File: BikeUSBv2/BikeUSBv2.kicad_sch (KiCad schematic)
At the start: 50 parts, among them J1 TYPE-C-31-M-16, J2 Conn_01x02_Female, Q1 MMBT3906, SW1 SW_Push, SW2 SW_Push, U1 TPS63020DSJR, U2 ATtiny1616-M

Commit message: all parts selected
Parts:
- D1: value yellow -> XL-2012UOC; LCSC (none) -> C965813
- D10: now not fitted; now left out of the parts list
- D2: value green -> XL-2012UGC; LCSC (none) -> C965815
- D3: value blue -> XL-2012UBC; LCSC (none) -> C965817
- D9: value red -> XL-2012SURC; LCSC (none) -> C965812
- J2: value Conn_01x02_Female -> JST S2B-EH(LF)(SN); LCSC (none) -> C514173
- SW1, SW2: value SW_Push -> 1TS002E-2500-2501-CT; LCSC (none) -> C255802
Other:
- moved on the sheet: SW1, SW2
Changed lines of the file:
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@@
     (stroke (width 0) (type default))
   )
-  (wire (pts (xy 103.505 181.61) (xy 106.68 181.61))
+  (wire (pts (xy 109.22 181.61) (xy 112.395 181.61))
     (stroke (width 0) (type default))
   )
@@
     (stroke (width 0) (type default))
   )
-  (wire (pts (xy 103.505 175.26) (xy 106.68 175.26))
+  (wire (pts (xy 109.22 175.26) (xy 112.395 175.26))
     (stroke (width 0) (type default))
   )
@@
     (effects (font (size 1.27 1.27)) (justify right bottom))
   )
-  (label "S2" (at 103.505 181.61 0) (fields_autoplaced)
+  (label "S2" (at 109.22 181.61 0) (fields_autoplaced)
     (effects (font (size 1.27 1.27)) (justify left bottom))
   )
@@
     (effects (font (size 1.27 1.27)) (justify right bottom))
   )
-  (label "S1" (at 103.505 175.26 0) (fields_autoplaced)
+  (label "S1" (at 109.22 175.26 0) (fields_autoplaced)
     (effects (font (size 1.27 1.27)) (justify left bottom))
   )
@@
       (effects (font (size 1.27 1.27)) (justify right))
     )
-    (property "Value" "red" (at 90.805 175.26 0)
+    (property "Value" "XL-2012SURC" (at 90.805 175.26 0)
       (effects (font (size 1.27 1.27)) (justify right))
     )
@@
       (effects (font (size 1.27 1.27)) hide)
     )
+    (property "LCSC" "C965812" (at 88.265 179.07 0)
+      (effects (font (size 1.27 1.27)) hide)
+    )
     (pin "2")
     (pin "1")
@@
   )
   (symbol (lib_id "Device:D_Schottky") (at 85.09 126.365 270) (unit 1)
-    (in_bom yes) (on_board yes) (dnp no)
+    (in_bom no) (on_board yes) (dnp yes)
     (property "Reference" "D10" (at 82.55 124.46 0)
       (effects (font (size 1.27 1.27)) (justify left))
@@
     )
   )
-  (symbol (lib_id "Switch:SW_Push") (at 111.76 181.61 0) (unit 1)
-    (in_bom yes) (on_board yes) (dnp no)
-    (property "Reference" "SW2" (at 111.76 183.515 0)
-      (effects (font (size 1.27 1.27)))
-    )
-    (property "Value" "SW_Push" (at 111.76 185.42 0)
-      (effects (font (size 1.27 1.27)))
-    )
-    (property "Footprint" "Button_Switch_SMD:SW_SPST_CK_RS282G05A3" (at 111.76 176.53 0)
-      (effects (font (size 1.27 1.27)) hide)
-    )
-    (property "Datasheet" "~" (at 111.76 176.53 0)
+  (symbol (lib_id "Switch:SW_Push") (at 117.475 181.61 0) (unit 1)
+    (in_bom yes) (on_board yes) (dnp no)
+    (property "Reference" "SW2" (at 117.475 183.515 0)
+      (effects (font (size 1.27 1.27)))
+    )
+    (property "Value" "1TS002E-2500-2501-CT" (at 117.475 185.42 0)
+      (effects (font (size 1.27 1.27)))
+    )
+    (property "Footprint" "Button_Switch_SMD:SW_SPST_CK_RS282G05A3" (at 117.475 176.53 0)
+      (effects (font (size 1.27 1.27)) hide)
+    )
+    (property "Datasheet" "~" (at 117.475 176.53 0)
+      (effects (font (size 1.27 1.27)) hide)
+    )
+    (property "LCSC" "C255802" (at 117.475 181.61 0)
       (effects (font (size 1.27 1.27)) hide)
     )
@@
       (effects (font (size 1.27 1.27)) (justify right))
     )
-    (property "Value" "green" (at 129.54 100.6475 90)
+    (property "Value" "XL-2012UGC" (at 129.54 100.6475 90)
       (effects (font (size 1.27 1.27)) (justify right))
     )
@@
     )
     (property "Datasheet" "~" (at 125.73 97.79 0)
+      (effects (font (size 1.27 1.27)) hide)
+    )
+    (property "LCSC" "C965815" (at 125.73 97.79 90)
       (effects (font (size 1.27 1.27)) hide)
     )
@@
     )
   )
-  (symbol (lib_id "Switch:SW_Push") (at 111.76 175.26 0) (unit 1)
-    (in_bom yes) (on_board yes) (dnp no)
-    (property "Reference" "SW1" (at 111.76 168.91 0)
-      (effects (font (size 1.27 1.27)))
-    )
-    (property "Value" "SW_Push" (at 111.76 170.815 0)
-      (effects (font (size 1.27 1.27)))
-    )
-    (property "Footprint" "Button_Switch_SMD:SW_SPST_CK_RS282G05A3" (at 111.76 170.18 0)
-      (effects (font (size 1.27 1.27)) hide)
-    )
-    (property "Datasheet" "~" (at 111.76 170.18 0)
+  (symbol (lib_id "Switch:SW_Push") (at 117.475 175.26 0) (unit 1)
+    (in_bom yes) (on_board yes) (dnp no)
+    (property "Reference" "SW1" (at 117.475 168.91 0)
+      (effects (font (size 1.27 1.27)))
+    )
+    (property "Value" "1TS002E-2500-2501-CT" (at 117.475 170.815 0)
+      (effects (font (size 1.27 1.27)))
+    )
+    (property "Footprint" "Button_Switch_SMD:SW_SPST_CK_RS282G05A3" (at 117.475 170.18 0)
+      (effects (font (size 1.27 1.27)) hide)
+    )
+    (property "Datasheet" "~" (at 117.475 170.18 0)
+      (effects (font (size 1.27 1.27)) hide)
+    )
+    (property "LCSC" "C255802" (at 117.475 175.26 0)
       (effects (font (size 1.27 1.27)) hide)
     )
@@
       (effects (font (size 1.27 1.27)) (justify right))
     )
-    (property "Value" "blue" (at 90.17 167.64 0)
+    (property "Value" "XL-2012UBC" (at 90.17 167.64 0)
       (effects (font (size 1.27 1.27)) (justify right))
     )
@@
     )
     (property "Datasheet" "~" (at 88.265 171.45 0)
+      (effects (font (size 1.27 1.27)) hide)
+    )
+    (property "LCSC" "C965817" (at 88.265 171.45 0)
       (effects (font (size 1.27 1.27)) hide)
     )
@@
     )
   )
-  (symbol (lib_id "power:GND") (at 116.84 181.61 90) (mirror x) (unit 1)
-    (in_bom yes) (on_board yes) (dnp no)
-    (property "Reference" "#PWR026" (at 123.19 181.61 0)
-      (effects (font (size 1.27 1.27)) hide)
-    )
-    (property "Value" "GND" (at 120.65 181.61 90)
+  (symbol (lib_id "power:GND") (at 122.555 181.61 90) (mirror x) (unit 1)
+    (in_bom yes) (on_board yes) (dnp no)
+    (property "Reference" "#PWR026" (at 128.905 181.61 0)
+      (effects (font (size 1.27 1.27)) hide)
+    )
+    (property "Value" "GND" (at 126.365 181.61 90)
       (effects (font (size 1.27 1.27)) (justify right))
     )
-    (property "Footprint" "" (at 116.84 181.61 0)
-      (effects (font (size 1.27 1.27)) hide)
-    )
-    (property "Datasheet" "" (at 116.84 181.61 0)
+    (property "Footprint" "" (at 122.555 181.61 0)
+      (effects (font (size 1.27 1.27)) hide)
+    )
+    (property "Datasheet" "" (at 122.555 181.61 0)
       (effects (font (size 1.27 1.27)) hide)
     )
@@
       (effects (font (size 1.27 1.27)) (justify left))
     )
-    (property "Value" "Conn_01x02_Female" (at 39.37 109.22 0)
+    (property "Value" "JST S2B-EH(LF)(SN)" (at 39.37 109.22 0)
       (effects (font (size 1.27 1.27)) (justify left))
     )
@@
     )
     (property "Datasheet" "~" (at 38.1 106.68 0)
+      (effects (font (size 1.27 1.27)) hide)
+    )
+    (property "LCSC" "C514173" (at 38.1 106.68 0)
       (effects (font (size 1.27 1.27)) hide)
     )
@@
     )
   )
-  (symbol (lib_id "power:GND") (at 116.84 175.26 90) (mirror x) (unit 1)
-    (in_bom yes) (on_board yes) (dnp no) (fields_autoplaced)
-    (property "Reference" "#PWR025" (at 123.19 175.26 0)
-      (effects (font (size 1.27 1.27)) hide)
-    )
-    (property "Value" "GND" (at 120.65 175.26 90)
+  (symbol (lib_id "power:GND") (at 122.555 175.26 90) (mirror x) (unit 1)
+    (in_bom yes) (on_board yes) (dnp no) (fields_autoplaced)
+    (property "Reference" "#PWR025" (at 128.905 175.26 0)
+      (effects (font (size 1.27 1.27)) hide)
+    )
+    (property "Value" "GND" (at 126.365 175.26 90)
       (effects (font (size 1.27 1.27)) (justify right))
     )
-    (property "Footprint" "" (at 116.84 175.26 0)
-      (effects (font (size 1.27 1.27)) hide)
-    )
-    (property "Datasheet" "" (at 116.84 175.26 0)
+    (property "Footprint" "" (at 122.555 175.26 0)
+      (effects (font (size 1.27 1.27)) hide)
+    )
+    (property "Datasheet" "" (at 122.555 175.26 0)
       (effects (font (size 1.27 1.27)) hide)
     )
@@
       (effects (font (size 1.27 1.27)) (justify right))
     )
-    (property "Value" "yellow" (at 30.48 132.3975 90)
+    (property "Value" "XL-2012UOC" (at 30.48 132.3975 90)
       (effects (font (size 1.27 1.27)) (justify right))
     )
@@
       (effects (font (size 1.27 1.27)) hide)
     )
+    (property "LCSC" "C965813" (at 26.67 129.54 90)
+      (effects (font (size 1.27 1.27)) hide)
+    )

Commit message: stuff
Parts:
- renumbered D9 to D4, D4 to D5, D5 to D6, D6 to D8, D8 to D9
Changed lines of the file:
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@@
   (symbol (lib_id "Device:LED") (at 88.265 179.07 180) (unit 1)
     (in_bom yes) (on_board yes) (dnp no)
-    (property "Reference" "D9" (at 86.36 175.26 0)
+    (property "Reference" "D4" (at 86.36 175.26 0)
       (effects (font (size 1.27 1.27)) (justify right))
     )
@@
       (project "BikeUSBv2"
         (path "/b4aff538-5116-4944-9d24-c26a88d7dfe8"
-          (reference "D9") (unit 1)
+          (reference "D4") (unit 1)
         )
       )
@@
   (symbol (lib_id "Device:D_Schottky") (at 23.495 84.455 270) (unit 1)
     (in_bom yes) (on_board yes) (dnp no)
-    (property "Reference" "D5" (at 25.4 84.455 90)
+    (property "Reference" "D6" (at 25.4 84.455 90)
       (effects (font (size 1.27 1.27)) (justify left))
     )
@@
       (project "BikeUSBv2"
         (path "/b4aff538-5116-4944-9d24-c26a88d7dfe8"
-          (reference "D5") (unit 1)
+          (reference "D6") (unit 1)
         )
       )
@@
   (symbol (lib_id "Device:D_Zener") (at 20.32 55.88 270) (unit 1)
     (in_bom yes) (on_board yes) (dnp no) (fields_autoplaced)
-    (property "Reference" "D8" (at 22.86 54.61 90)
+    (property "Reference" "D9" (at 22.86 54.61 90)
       (effects (font (size 1.27 1.27)) (justify left))
     )
@@
       (project "BikeUSBv2"
         (path "/b4aff538-5116-4944-9d24-c26a88d7dfe8"
-          (reference "D8") (unit 1)
+          (reference "D9") (unit 1)
         )
       )
@@
   (symbol (lib_id "Device:D_Schottky") (at 23.495 92.075 270) (unit 1)
     (in_bom yes) (on_board yes) (dnp no)
-    (property "Reference" "D4" (at 25.4 92.075 90)
+    (property "Reference" "D5" (at 25.4 92.075 90)
       (effects (font (size 1.27 1.27)) (justify left))
     )
@@
       (project "BikeUSBv2"
         (path "/b4aff538-5116-4944-9d24-c26a88d7dfe8"
-          (reference "D4") (unit 1)
+          (reference "D5") (unit 1)
         )
       )
@@
   (symbol (lib_id "Device:D_Schottky") (at 35.56 84.455 270) (unit 1)
     (in_bom yes) (on_board yes) (dnp no)
-    (property "Reference" "D6" (at 31.115 84.455 90)
+    (property "Reference" "D8" (at 31.115 84.455 90)
       (effects (font (size 1.27 1.27)) (justify left))
     )
@@
       (project "BikeUSBv2"
         (path "/b4aff538-5116-4944-9d24-c26a88d7dfe8"
-          (reference "D6") (unit 1)
-        )
-      )
+          (reference "D8") (unit 1)
+        )
+      )

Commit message: lcsc parts
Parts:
- C1, C10, C11, C8: LCSC (none) -> C1711
- C2, C3, C4: LCSC (none) -> C1779
- C5, C6, C7: LCSC (none) -> C12891
- C9: LCSC (none) -> C178661
- D5, D6, D7, D8: LCSC (none) -> C603062
- D9: LCSC (none) -> C7422622
- J1: LCSC (none) -> C283541
- L1: LCSC (none) -> C338840
- Q1: LCSC (none) -> C2891809
- R1, R10, R11, R2, R3, R4, R5: LCSC (none) -> C218592
- R12, R13, R14, R7, R8, R9: LCSC (none) -> C706357
- U1: LCSC (none) -> C15483
- U2: LCSC (none) -> C507118
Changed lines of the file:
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@@
+      (effects (font (size 1.27 1.27)) hide)
+    )
+    (property "LCSC" "C218592" (at 148.59 71.12 0)
       (effects (font (size 1.27 1.27)) hide)
     )
@@
       (effects (font (size 1.27 1.27)) hide)
     )
+    (property "LCSC" "C706357" (at 24.13 121.92 0)
+      (effects (font (size 1.27 1.27)) hide)
+    )
     (pin "1")
     (pin "2")
@@
       (effects (font (size 1.27 1.27)) hide)
     )
+    (property "LCSC" "C706357" (at 80.645 181.61 0)
+      (effects (font (size 1.27 1.27)) hide)
+    )
     (pin "1")
     (pin "2")
@@
     )
     (property "LCSC Part" "C2891809" (at 157.48 73.66 0)
+      (effects (font (size 1.27 1.27)) hide)
+    )
+    (property "LCSC" "C2891809" (at 162.56 74.93 0)
       (effects (font (size 1.27 1.27)) hide)
     )
@@
       (effects (font (size 1.27 1.27)) hide)
     )
+    (property "LCSC" "C603062" (at 25.4 84.455 0)
+      (effects (font (size 1.27 1.27)) hide)
+    )
     (pin "2")
     (pin "1")
@@
       (effects (font (size 1.27 1.27)) hide)
     )
+    (property "LCSC" "C7422622" (at 22.86 54.61 0)
+      (effects (font (size 1.27 1.27)) hide)
+    )
     (pin "1")
     (pin "2")
@@
     )
     (property "Sim.Pins" "1=K 2=A" (at 35.56 92.075 0)
+      (effects (font (size 1.27 1.27)) hide)
+    )
+    (property "LCSC" "C603062" (at 31.115 92.075 0)
       (effects (font (size 1.27 1.27)) hide)
     )
@@
       (effects (font (size 1.27 1.27)) hide)
     )
+    (property "LCSC" "C1711" (at 120.65 56.515 0)
+      (effects (font (size 1.27 1.27)) hide)
+    )
     (pin "1")
     (pin "2")
@@
     )
     (property "Datasheet" "https://www.usb.org/sites/default/files/documents/usb_type-c.zip" (at 209.55 92.71 0)
+      (effects (font (size 1.27 1.27)) hide)
+    )
+    (property "LCSC" "C283541" (at 208.28 76.2 0)
       (effects (font (size 1.27 1.27)) hide)
     )
@@
       (effects (font (size 1.27 1.27)) hide)
     )
+    (property "LCSC" "C1711" (at 55.245 95.25 0)
+      (effects (font (size 1.27 1.27)) hide)
+    )
     (pin "1")
     (pin "2")
@@
     )
     (property "Datasheet" "~" (at 77.47 118.745 0)
+      (effects (font (size 1.27 1.27)) hide)
+    )
+    (property "LCSC" "C218592" (at 74.93 118.745 0)
       (effects (font (size 1.27 1.27)) hide)
     )
@@
       (effects (font (size 1.27 1.27)) hide)
     )
+    (property "LCSC" "C1711" (at 66.04 59.69 0)
+      (effects (font (size 1.27 1.27)) hide)
+    )
     (pin "1")
     (pin "2")
@@
       (effects (font (size 1.27 1.27)) hide)
     )
+    (property "LCSC" "C603062" (at 25.4 92.075 0)
+      (effects (font (size 1.27 1.27)) hide)
+    )
     (pin "2")
     (pin "1")
@@
       (effects (font (size 1.27 1.27)) hide)
     )
+    (property "LCSC" "C1711" (at 151.13 56.515 0)
+      (effects (font (size 1.27 1.27)) hide)
+    )
     (pin "1")
     (pin "2")
@@
       (effects (font (size 1.27 1.27)) hide)
     )
+    (property "LCSC" "C218592" (at 157.48 92.71 0)
+      (effects (font (size 1.27 1.27)) hide)
+    )
     (pin "1")
     (pin "2")
@@
       (effects (font (size 1.27 1.27)) hide)
     )
+    (property "LCSC" "C706357" (at 80.645 173.99 0)
+      (effects (font (size 1.27 1.27)) hide)
+    )
     (pin "1")
     (pin "2")
@@
       (effects (font (size 1.27 1.27)) hide)
     )
+    (property "LCSC" "C338840" (at 74.295 97.79 0)
+      (effects (font (size 1.27 1.27)) hide)
+    )
     (pin "1")
     (pin "2")
@@
       (effects (font (size 1.27 1.27)) hide)
     )
+    (property "LCSC" "C218592" (at 172.72 92.71 0)
+      (effects (font (size 1.27 1.27)) hide)
+    )
     (pin "1")
     (pin "2")
@@
       (effects (font (size 1.27 1.27)) hide)
     )
+    (property "LCSC" "C12891" (at 131.445 56.515 0)
+      (effects (font (size 1.27 1.27)) hide)
+    )
     (pin "1")
     (pin "2")
@@
       (effects (font (size 1.27 1.27)) hide)
     )
+    (property "LCSC" "C218592" (at 162.56 92.71 0)
+      (effects (font (size 1.27 1.27)) hide)
+    )
     (pin "1")
     (pin "2")
@@
     )
     (property "Datasheet" "~" (at 101.6 60.96 0)
+      (effects (font (size 1.27 1.27)) hide)
+    )
+    (property "LCSC" "C12891" (at 105.41 59.69 0)
       (effects (font (size 1.27 1.27)) hide)
     )
@@
     )
     (property "LCSC Part" "C15483" (at 93.345 120.015 0)
+      (effects (font (size 1.27 1.27)) hide)
+    )
+    (property "LCSC" "C15483" (at 93.345 76.835 0)
       (effects (font (size 1.27 1.27)) hide)
     )
@@
     )
     (property "Datasheet" "http://ww1.microchip.com/downloads/en/DeviceDoc/ATtiny3216_ATtiny1616-data-sheet-40001997B.pdf" (at 55.88 163.83 0)
+      (effects (font (size 1.27 1.27)) hide)
+    )
+    (property "LCSC" "C507118" (at 58.0741 138.43 0)
       (effects (font (size 1.27 1.27)) hide)
     )
@@
       (effects (font (size 1.27 1.27)) hide)
     )
+    (property "LCSC" "C1779" (at 85.09 59.69 0)
+      (effects (font (size 1.27 1.27)) hide)
+    )
     (pin "1")
     (pin "2")
@@
       (effects (font (size 1.27 1.27)) hide)
     )
+    (property "LCSC" "C218592" (at 114.3 86.995 0)
+      (effects (font (size 1.27 1.27)) hide)
+    )
     (pin "1")
     (pin "2")
@@
       (effects (font (size 1.27 1.27)) hide)
     )
+    (property "LCSC" "C706357" (at 74.93 126.365 0)
+      (effects (font (size 1.27 1.27)) hide)
+    )
     (pin "1")
     (pin "2")
@@
     )
     (property "Datasheet" "~" (at 116.84 94.615 0)
+      (effects (font (size 1.27 1.27)) hide)
+    )
+    (property "LCSC" "C706357" (at 114.3 94.615 0)
       (effects (font (size 1.27 1.27)) hide)
     )
@@
     )
     (property "Sim.Pins" "1=K 2=A" (at 35.56 84.455 0)
+      (effects (font (size 1.27 1.27)) hide)
+    )
+    (property "LCSC" "C603062" (at 31.115 84.455 0)
       (effects (font (size 1.27 1.27)) hide)
     )
@@
       (effects (font (size 1.27 1.27)) hide)
     )
+    (property "LCSC" "C1779" (at 75.565 59.69 0)
+      (effects (font (size 1.27 1.27)) hide)
+    )
     (pin "1")
     (pin "2")
@@
       (effects (font (size 1.27 1.27)) hide)
     )
+    (property "LCSC" "C706357" (at 123.19 90.17 0)
+      (effects (font (size 1.27 1.27)) hide)
+    )
     (pin "1")
     (pin "2")
@@
     )
     (property "Datasheet" "~" (at 138.43 57.785 0)
+      (effects (font (size 1.27 1.27)) hide)
+    )
+    (property "LCSC" "C12891" (at 140.97 56.515 0)
       (effects (font (size 1.27 1.27)) hide)
     )
@@
       (effects (font (size 1.27 1.27)) hide)
     )
+    (property "LCSC" "C178661" (at 48.26 70.231 0)
+      (effects (font (size 1.27 1.27)) hide)
+    )
     (pin "1")
     (pin "2")
@@
       (effects (font (size 1.27 1.27)) hide)
     )
+    (property "LCSC" "C218592" (at 167.64 92.71 0)
+      (effects (font (size 1.27 1.27)) hide)
+    )
     (pin "1")
     (pin "2")
@@
       (effects (font (size 1.27 1.27)) hide)
     )
+    (property "LCSC" "C1779" (at 94.615 59.69 0)
+      (effects (font (size 1.27 1.27)) hide)
+    )

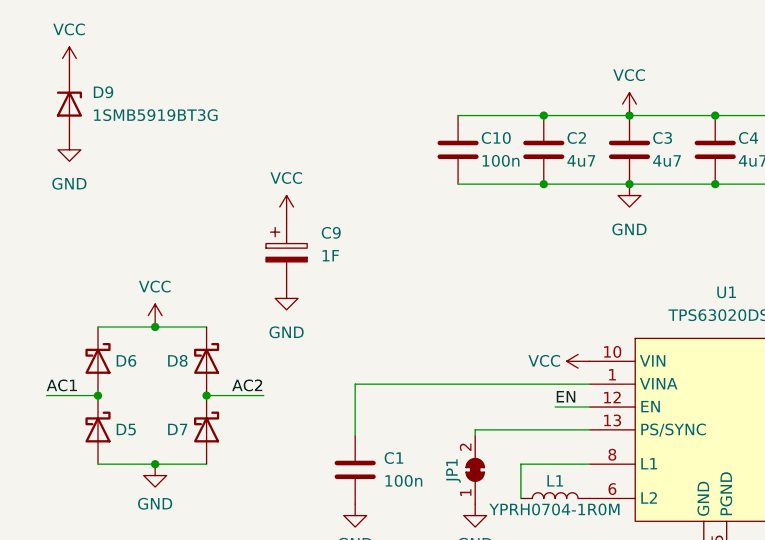
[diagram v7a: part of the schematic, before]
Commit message: half capacitance, but cheaper
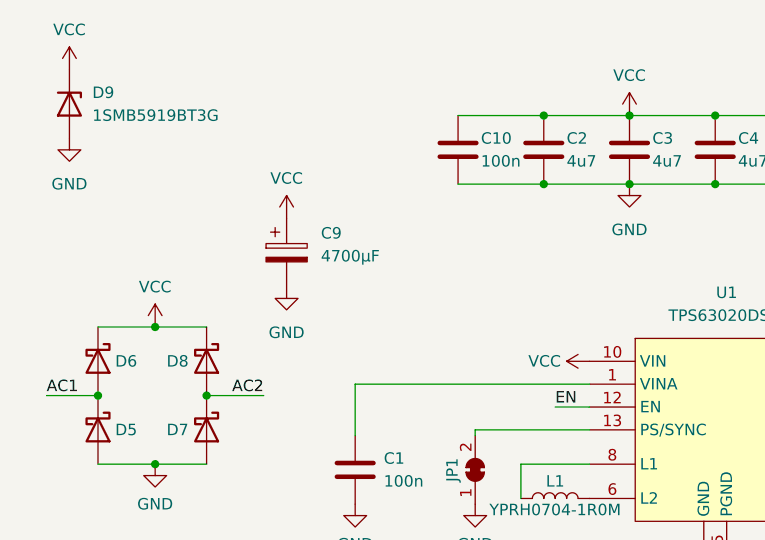
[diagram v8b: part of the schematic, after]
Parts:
- C9: value 1F -> 4700µF; LCSC C178661 -> C47893
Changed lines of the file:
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@@
   )
   (symbol (lib_id "Device:C_Polarized") (at 44.45 72.39 0) (unit 1)
-    (in_bom yes) (on_board yes) (dnp no) (fields_autoplaced)
+    (in_bom yes) (on_board yes) (dnp no)
     (property "Reference" "C9" (at 48.26 70.231 0)
       (effects (font (size 1.27 1.27)) (justify left))
     )
-    (property "Value" "1F" (at 48.26 72.771 0)
+    (property "Value" "4700µF" (at 48.26 72.771 0)
       (effects (font (size 1.27 1.27)) (justify left))
     )
@@
       (effects (font (size 1.27 1.27)) hide)
     )
-    (property "LCSC" "C178661" (at 48.26 70.231 0)
+    (property "LCSC" "C47893" (at 48.26 70.231 0)
       (effects (font (size 1.27 1.27)) hide)
     )
